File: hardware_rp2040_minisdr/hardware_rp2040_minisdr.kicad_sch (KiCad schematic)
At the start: 48 parts, among them IC1 PSA4-5043+, IC2 ADE-11X+, IC3 SI5351A-B-GTR, IC4 GALI-84+, IC5 ADCS7476AIMFX_NOPB, J1 Conn_Coaxial_Small, J2 USB_A, SW1 SW_Push, U1 RP2040, U2 W25Q128JVS, U3 AMS1117-3.3, Y1 Crystal_GND24, Y2 Crystal_GND24

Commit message: LEDs
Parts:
- J2: footprint (none) -> user_imported_devices:USBPCB
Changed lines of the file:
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@@
 			)
 		)
-		(property "Footprint" ""
+		(property "Footprint" "user_imported_devices:USBPCB"
 			(at 44.45 52.07 0)
 			(effects

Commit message: board
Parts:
- added C1: 100n, Capacitor_SMD:C_0402_1005Metric, symbol Device:C
- added R1, R7: 10k, Resistor_SMD:R_0402_1005Metric, symbol Device:R
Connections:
- net 3v3: now also R1.2
- net GND: now also C1.1, R7.1
- net at C26.1, IC5.3 (VIN): now also C1.2, R1.1, R7.2
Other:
- moved on the sheet: IC5

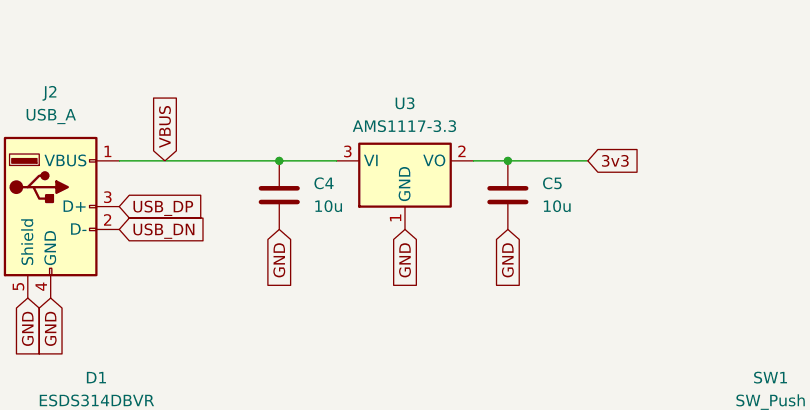
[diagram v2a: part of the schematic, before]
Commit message: pcb placement
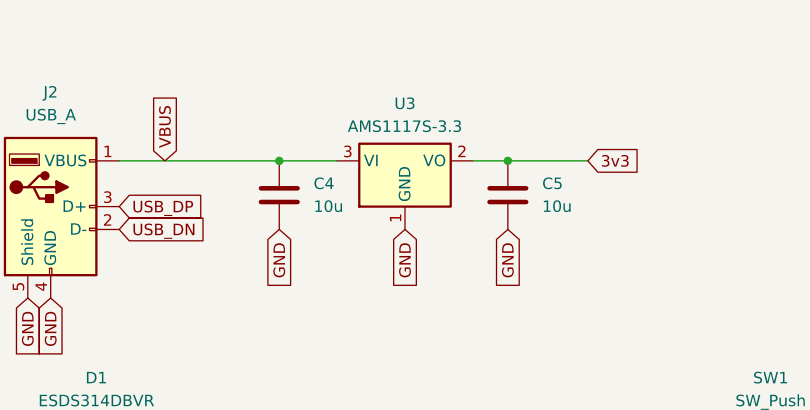
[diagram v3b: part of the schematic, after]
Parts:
- U3: value AMS1117-3.3 -> AMS1117S-3.3; footprint Package_TO_SOT_SMD:SOT-223-3_TabPin2 -> Package_TO_SOT_SMD:SOT-89-3
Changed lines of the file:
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@@
 			)
 		)
-		(property "Value" "AMS1117-3.3"
+		(property "Value" "AMS1117S-3.3"
 			(at 80.01 41.91 0)
 			(effects
@@
 			)
 		)
-		(property "Footprint" "Package_TO_SOT_SMD:SOT-223-3_TabPin2"
+		(property "Footprint" "Package_TO_SOT_SMD:SOT-89-3"
 			(at 80.01 40.64 0)
 			(effects

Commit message: pcb
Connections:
- net at IC3.10 (CLK0): no longer C20.1
- net at IC3.6 (CLK2): now also C20.1
- no-connect marks 0 -> 27
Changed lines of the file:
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@@
 		(color 0 0 0 0)
 	)
+	(no_connect
+		(at 228.6 81.28)
+	)
+	(no_connect
+		(at 228.6 119.38)
+	)
+	(no_connect
+		(at 228.6 88.9)
+	)
+	(no_connect
+		(at 228.6 78.74)
+	)
+	(no_connect
+		(at 228.6 86.36)
+	)
+	(no_connect
+		(at 228.6 144.78)
+	)
+	(no_connect
+		(at 157.48 151.13)
+	)
+	(no_connect
+		(at 228.6 129.54)
+	)
+	(no_connect
+		(at 228.6 142.24)
+	)
+	(no_connect
+		(at 228.6 68.58)
+	)
+	(no_connect
+		(at 228.6 132.08)
+	)
+	(no_connect
+		(at 228.6 127)
+	)
+	(no_connect
+		(at 228.6 99.06)
+	)
+	(no_connect
+		(at 228.6 114.3)
+	)
+	(no_connect
+		(at 228.6 106.68)
+	)
+	(no_connect
+		(at 228.6 73.66)
+	)
+	(no_connect
+		(at 228.6 139.7)
+	)
+	(no_connect
+		(at 228.6 101.6)
+	)
+	(no_connect
+		(at 228.6 83.82)
+	)
+	(no_connect
+		(at 228.6 124.46)
+	)
+	(no_connect
+		(at 157.48 148.59)
+	)
+	(no_connect
+		(at 228.6 71.12)
+	)
+	(no_connect
+		(at 228.6 116.84)
+	)
+	(no_connect
+		(at 228.6 137.16)
+	)
+	(no_connect
+		(at 228.6 121.92)
+	)
+	(no_connect
+		(at 228.6 76.2)
+	)
+	(no_connect
+		(at 228.6 104.14)
+	)
 	(wire
 		(pts
@@
 	(wire
 		(pts
+			(xy 166.37 144.78) (xy 166.37 158.75)
+		)
+		(stroke
+			(width 0)
+			(type default)
+		)
+	)
+	(wire
+		(pts
 			(xy 107.95 147.32) (xy 121.92 147.32)
 		)
@@
 	(wire
 		(pts
-			(xy 152.4 144.78) (xy 157.48 144.78)
-		)
-		(stroke
-			(width 0)
-			(type default)
-		)
-	)
-	(wire
-		(pts
 			(xy 38.1 106.68) (xy 41.91 106.68)
 		)
@@
 	(wire
 		(pts
+			(xy 152.4 144.78) (xy 166.37 144.78)
+		)
+		(stroke
+			(width 0)
+			(type default)
+		)
+	)
+	(wire
+		(pts
 			(xy 213.36 36.83) (xy 215.9 36.83)
 		)
@@
 	(wire
 		(pts
-			(xy 157.48 144.78) (xy 157.48 148.59)
-		)
-		(stroke
-			(width 0)
-			(type default)
-		)
-	)
-	(wire
-		(pts
 			(xy 186.69 36.83) (xy 186.69 40.64)
 		)
@@
 		)
 		(stroke
+			(width 0)
+			(type default)
+		)
+	)
+	(wire
+		(pts
+			(xy 166.37 158.75) (xy 157.48 158.75)
+		)
+		(stroke

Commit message: pcb
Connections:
- net at IC3.10 (CLK0): now also C20.1
- net at IC3.6 (CLK2): no longer C20.1
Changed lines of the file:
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@@
-	)
-	(no_connect
-		(at 157.48 148.59)
 	)
 	(no_connect
@@
 	)
 	(no_connect
+		(at 157.48 158.75)
+	)
+	(no_connect
 		(at 228.6 104.14)
 	)
@@
 	(wire
 		(pts
+			(xy 152.4 144.78) (xy 157.48 144.78)
+		)
+		(stroke
+			(width 0)
+			(type default)
+		)
+	)
+	(wire
+		(pts
 			(xy 154.94 124.46) (xy 167.64 124.46)
 		)
@@
 	(wire
 		(pts
-			(xy 166.37 144.78) (xy 166.37 158.75)
-		)
-		(stroke
-			(width 0)
-			(type default)
-		)
-	)
-	(wire
-		(pts
 			(xy 107.95 147.32) (xy 121.92 147.32)
 		)
@@
 	(wire
 		(pts
-			(xy 152.4 144.78) (xy 166.37 144.78)
-		)
-		(stroke
-			(width 0)
-			(type default)
-		)
-	)
-	(wire
-		(pts
 			(xy 213.36 36.83) (xy 215.9 36.83)
 		)
@@
 	(wire
 		(pts
+			(xy 157.48 144.78) (xy 157.48 148.59)
+		)
+		(stroke
+			(width 0)
+			(type default)
+		)
+	)
+	(wire
+		(pts
 			(xy 93.98 109.22) (xy 99.06 109.22)
 		)
@@
 		)
 		(stroke
-			(width 0)
-			(type default)
-		)
-	)
-	(wire
-		(pts
-			(xy 166.37 158.75) (xy 157.48 158.75)
-		)
-		(stroke

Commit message: pcb hardware!
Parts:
- J2: footprint user_imported_devices:USBPCB -> Connector_USB:USB_A_Connfly_DS1098_Horizontal
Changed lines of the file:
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@@
 			)
 		)
-		(property "Footprint" "user_imported_devices:USBPCB"
+		(property "Footprint" "Connector_USB:USB_A_Connfly_DS1098_Horizontal"
 			(at 44.45 52.07 0)
 			(effects
